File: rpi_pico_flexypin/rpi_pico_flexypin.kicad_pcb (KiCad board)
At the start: 2 copper layers, 72.2 x 90 mm, 20 parts, among them J1 Conn_01x20, J2 Conn_01x03, J3 Conn_01x20, J4 Conn_01x17, J5 Conn_01x17, J6 Conn_Debug, SW1 SW_RST, U1 RaspberryPi_Pico

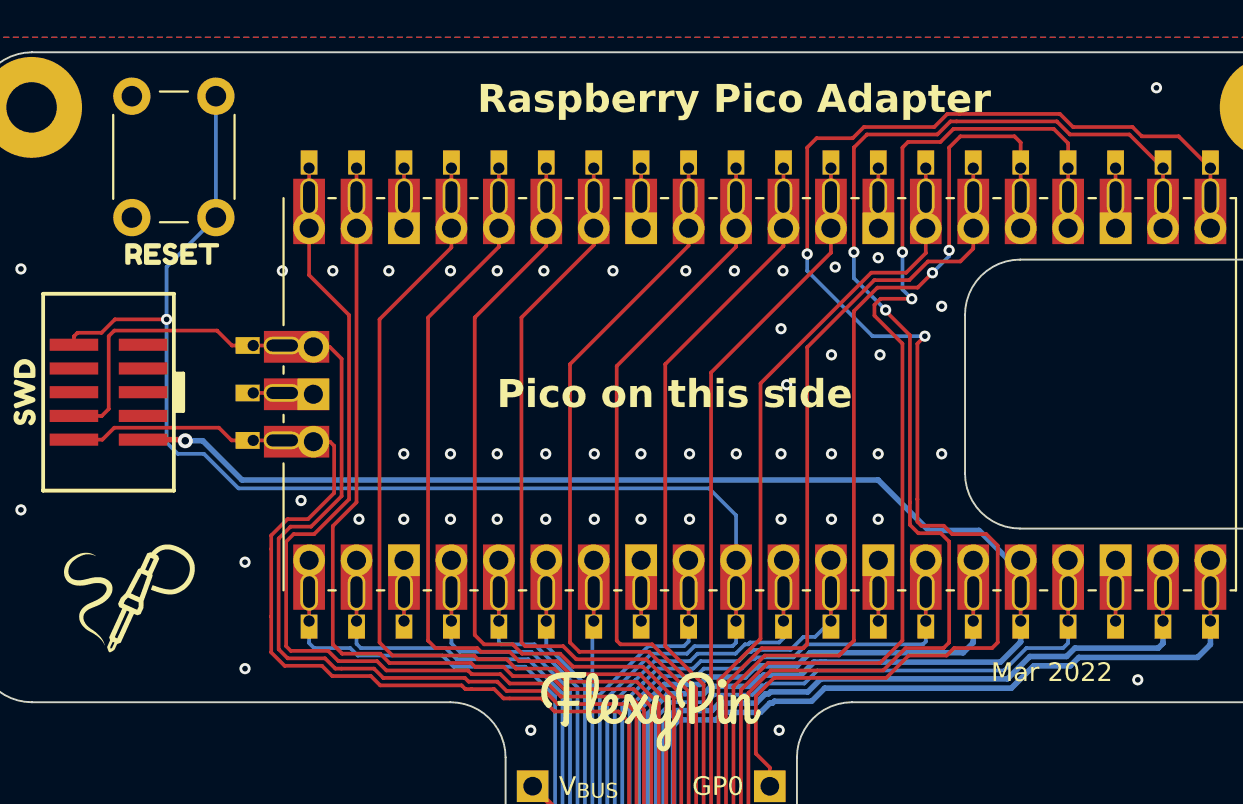
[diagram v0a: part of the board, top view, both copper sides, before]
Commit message: Change Pico Adapters' Reset Button to SMD
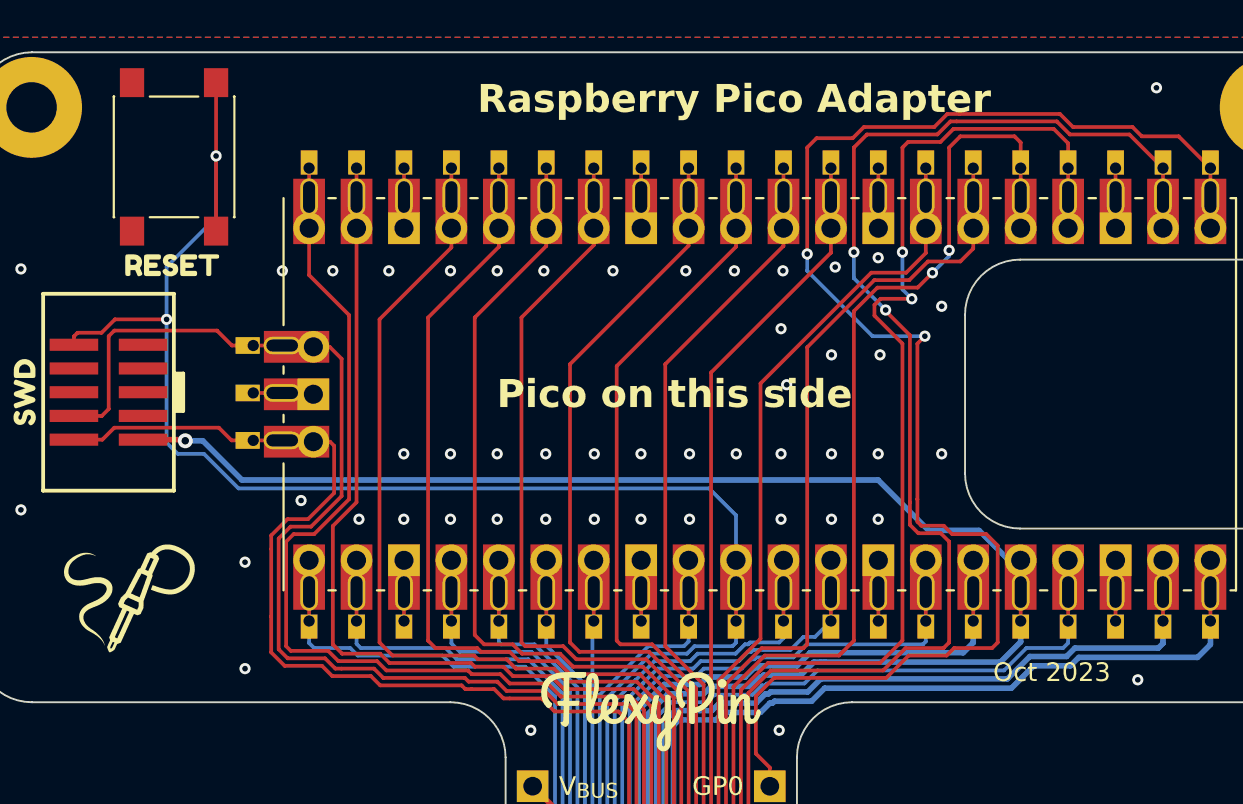
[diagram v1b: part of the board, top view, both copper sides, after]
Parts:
- SW1: footprint Button_Switch_THT:SW_PUSH_6mm -> Button_Switch_SMD:SW_Push_1P1T_NO_6x6mm_H9.5mm
- moved SW1 3.96 mm to (105.2, 77.3)
- moved kibuzzard-6227DBF8 0.60 mm to (105.1, 83.1)
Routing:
- net /RUN: track 124.4 -> 129.2 mm, vias 2 -> 3
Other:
- board text added: "Oct 2023"
- board text removed: "Mar 2022"
